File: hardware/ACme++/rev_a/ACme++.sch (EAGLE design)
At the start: 89 parts, among them J1 AC-PLUG, J2 WIRE_HOLE-14AWG, J3 TC2030-CTX-NL, J4 WIRE_HOLE-14AWG, J5 WIRE_HOLE-14AWG, K1 S216S01F, Q1 STGD5NB120SZT4, Q2 FDV301N, U1 ADE7753, U2 SR086SG-G, U3 TDA3664AT, U4 FM25LBTDFN-8, U5 CC2538, U6 DS2411, U7 TXB0104RGY, X1 ECS-35-17-5PX-TR, X2 EPSON-FA-128, X3 FC-12M32.7680KA-A3

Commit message: routing and labeling
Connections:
- net LOAD_PHASE: now also K1.1; no longer K1.2
- net WALL_PHASE: now also K1.2; no longer K1.1
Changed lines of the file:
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@@
+</segment>
+<segment>
+<pinref part="J1" gate="G$1" pin="PHASE"/>
+<wire x1="157.48" y1="170.18" x2="160.02" y2="170.18" width="0.1524" layer="91"/>
+<label x="160.02" y="170.18" size="1.27" layer="95" xref="yes"/>
+</segment>
+<segment>
+<pinref part="K1" gate="G$1" pin="2"/>
+<wire x1="63.5" y1="30.48" x2="66.04" y2="30.48" width="0.1524" layer="91"/>
+<label x="66.04" y="30.48" size="1.27" layer="95" xref="yes"/>
+</segment>
+</net>
+<net name="LOAD_PHASE" class="0">
+<segment>
+<pinref part="J2" gate="G$1" pin="P$1"/>
+<wire x1="220.98" y1="170.18" x2="218.44" y2="170.18" width="0.1524" layer="91"/>
+<label x="218.44" y="170.18" size="1.27" layer="95" rot="R180" xref="yes"/>
 </segment>
 <segment>
@@
 <label x="66.04" y="35.56" size="1.27" layer="95" xref="yes"/>
 </segment>
-<segment>
-<pinref part="J1" gate="G$1" pin="PHASE"/>
-<wire x1="157.48" y1="170.18" x2="160.02" y2="170.18" width="0.1524" layer="91"/>
-<label x="160.02" y="170.18" size="1.27" layer="95" xref="yes"/>
-</segment>
 </net>
-<net name="LOAD_PHASE" class="0">
-<segment>
-<pinref part="K1" gate="G$1" pin="2"/>
-<wire x1="63.5" y1="30.48" x2="66.04" y2="30.48" width="0.1524" layer="91"/>
-<label x="66.04" y="30.48" size="1.27" layer="95" xref="yes"/>
-</segment>
-<segment>
-<pinref part="J2" gate="G$1" pin="P$1"/>
-<wire x1="220.98" y1="170.18" x2="218.44" y2="170.18" width="0.1524" layer="91"/>
-<label x="218.44" y="170.18" size="1.27" layer="95" rot="R180" xref="yes"/>
-</segment>
-</net>

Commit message: added labels to schematic
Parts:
- added U$3: UMICH_SOLID_MEDIUM, logos:UMICH_SOLID_MEDIUM
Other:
- note added: "AC Plugs"
- note added: "ADE7753 Power Measurement"
- note added: "CC2538"
- note added: "DS2411"
- note added: "FRAM"
- note added: "Level Converter 5V SPI"
- note added: "Load Control Relay"
- note added: "Metering Conditioning"
- note added: "Programmer Header"
- note added: "Relay Control Switch and LED"

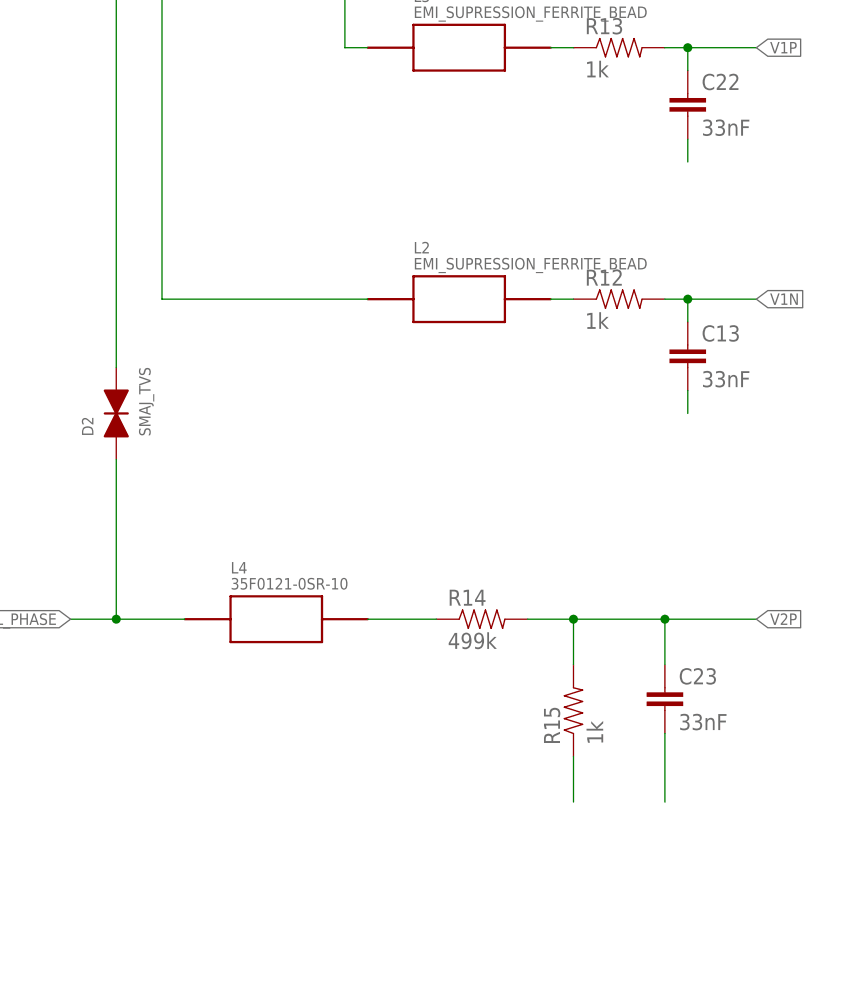
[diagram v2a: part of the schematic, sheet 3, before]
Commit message: changed gnd and routed
made the gnd for the ade measurement signals the emi filtered neutral
from the wall. As best as I can tell this is was acme does. Updated that
on the schematic and routed it.
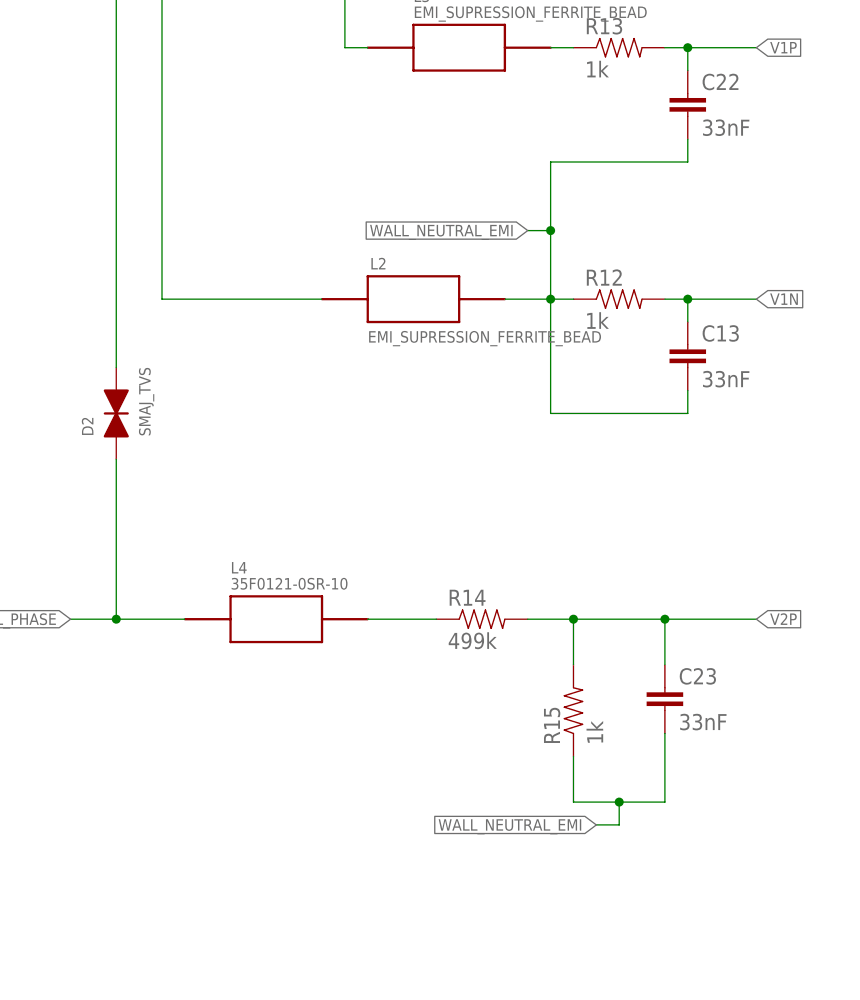
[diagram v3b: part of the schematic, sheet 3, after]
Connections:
- removed net N$14: L2.P$2, R12.1
- removed net N$19: C22.2
- removed net N$23: C13.2
- removed net N$25: C23.2
- removed net N$27: R15.1
- new net WALL_NEUTRAL_EMI: C13.2, C22.2, C23.2, L2.P$2, R12.1, R15.1
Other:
- moved on the sheet: L2
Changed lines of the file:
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@@
 <attribute name="DIGIKEY" x="152.4" y="157.48" size="1.27" layer="96" display="off"/>
 </instance>
-<instance part="L2" gate="G$1" x="177.8" y="119.38"/>
+<instance part="L2" gate="G$1" x="172.72" y="119.38" smashed="yes">
+<attribute name="NAME" x="167.894" y="122.682" size="1.27" layer="95"/>
+<attribute name="VALUE" x="167.64" y="114.554" size="1.27" layer="96"/>
+</instance>
 <instance part="L3" gate="G$1" x="177.8" y="147.32"/>
 <instance part="R12" gate="G$1" x="195.58" y="119.38">
@@
 <wire x1="144.78" y1="157.48" x2="139.7" y2="157.48" width="0.1524" layer="91"/>
 <wire x1="139.7" y1="157.48" x2="134.62" y2="157.48" width="0.1524" layer="91"/>
-<wire x1="167.64" y1="119.38" x2="144.78" y2="119.38" width="0.1524" layer="91"/>
+<wire x1="162.56" y1="119.38" x2="144.78" y2="119.38" width="0.1524" layer="91"/>
 <wire x1="144.78" y1="119.38" x2="144.78" y2="157.48" width="0.1524" layer="91"/>
 <junction x="144.78" y="157.48"/>
@@
 </segment>
 </net>
-<net name="N$14" class="0">
+<net name="WALL_NEUTRAL_EMI" class="0">
 <segment>
 <pinref part="L2" gate="G$1" pin="P$2"/>
 <pinref part="R12" gate="G$1" pin="1"/>
+<wire x1="182.88" y1="119.38" x2="187.96" y2="119.38" width="0.1524" layer="91"/>
 <wire x1="187.96" y1="119.38" x2="190.5" y2="119.38" width="0.1524" layer="91"/>
+<wire x1="187.96" y1="119.38" x2="187.96" y2="127" width="0.1524" layer="91"/>
+<wire x1="187.96" y1="127" x2="185.42" y2="127" width="0.1524" layer="91"/>
+<junction x="187.96" y="119.38"/>
+<label x="185.42" y="127" size="1.27" layer="95" rot="R180" xref="yes"/>
+<pinref part="C22" gate="G$1" pin="2"/>
+<wire x1="203.2" y1="137.16" x2="203.2" y2="134.62" width="0.1524" layer="91"/>
+<wire x1="187.96" y1="127" x2="187.96" y2="134.62" width="0.1524" layer="91"/>
+<wire x1="187.96" y1="134.62" x2="203.2" y2="134.62" width="0.1524" layer="91"/>
+<junction x="187.96" y="127"/>
+<pinref part="C13" gate="G$1" pin="2"/>
+<wire x1="203.2" y1="109.22" x2="203.2" y2="106.68" width="0.1524" layer="91"/>
+<wire x1="187.96" y1="119.38" x2="187.96" y2="106.68" width="0.1524" layer="91"/>
+<wire x1="187.96" y1="106.68" x2="203.2" y2="106.68" width="0.1524" layer="91"/>
+</segment>
+<segment>
+<pinref part="C23" gate="G$1" pin="2"/>
+<wire x1="200.66" y1="71.12" x2="200.66" y2="63.5" width="0.1524" layer="91"/>
+<pinref part="R15" gate="G$1" pin="1"/>
+<wire x1="190.5" y1="68.58" x2="190.5" y2="63.5" width="0.1524" layer="91"/>
+<wire x1="200.66" y1="63.5" x2="195.58" y2="63.5" width="0.1524" layer="91"/>
+<wire x1="195.58" y1="63.5" x2="190.5" y2="63.5" width="0.1524" layer="91"/>
+<wire x1="195.58" y1="63.5" x2="195.58" y2="60.96" width="0.1524" layer="91"/>
+<junction x="195.58" y="63.5"/>
+<wire x1="195.58" y1="60.96" x2="193.04" y2="60.96" width="0.1524" layer="91"/>
+<label x="193.04" y="60.96" size="1.27" layer="95" rot="R180" xref="yes"/>
 </segment>
 </net>
@@
 </segment>
 </net>
-<net name="N$19" class="0">
-<segment>
-<pinref part="C22" gate="G$1" pin="2"/>
-<wire x1="203.2" y1="137.16" x2="203.2" y2="134.62" width="0.1524" layer="91"/>
-</segment>
-</net>
-<net name="N$23" class="0">
-<segment>
-<pinref part="C13" gate="G$1" pin="2"/>
-<wire x1="203.2" y1="109.22" x2="203.2" y2="106.68" width="0.1524" layer="91"/>
-</segment>
-</net>
-<net name="N$25" class="0">
-<segment>
-<pinref part="C23" gate="G$1" pin="2"/>
-<wire x1="200.66" y1="71.12" x2="200.66" y2="63.5" width="0.1524" layer="91"/>
-</segment>
-</net>
-<net name="N$27" class="0">
-<segment>
-<pinref part="R15" gate="G$1" pin="1"/>
-<wire x1="190.5" y1="68.58" x2="190.5" y2="63.5" width="0.1524" layer="91"/>
-</segment>
-</net>

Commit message: routed ac under board, renamed
did my thing where part numbers correspond to values
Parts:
- added C36, C37: (no value), powercube:CAP_POL
- C1: value 0.1uF -> 12pF; device rcl:C-EUC0603 -> passives:CAPACITOR; DIGIKEY 445-1316-1-ND -> 445-1236-1-ND
- C10: value 0.1uF -> 33nF; device SparkFun-Passives:CAP0603-CAP -> SparkFun-Passives:CAP0805; DIGIKEY 445-1316-1-ND -> 478-1389-1-ND
- C11: value 47uF -> 0.1uF; device SparkFun-Passives:CAP1206 -> passives:CAPACITOR; DIGIKEY 399-5508-1-ND -> 445-1265-1-ND
- C12, C16: value 12pF -> 0.1uF; DIGIKEY 445-1236-1-ND -> 445-1265-1-ND
- C13: value 33nF -> 0.1uF; device SparkFun-Passives:CAP0805 -> passives:CAPACITOR; DIGIKEY 478-1389-1-ND -> 445-1265-1-ND
- C14: value 10uF -> 0.1uF; device rcl:C-EUC0603 -> passives:CAPACITOR; DIGIKEY (none) -> 445-1265-1-ND
- C15, C17: value 22pF -> 0.1uF; device rcl:C-EUC0603 -> passives:CAPACITOR; DIGIKEY (none) -> 445-1265-1-ND
- C18: value 1uF -> 0.1uF; DIGIKEY 445-4998-1-ND -> 445-1265-1-ND
- C2: value 10uF -> 12pF; device rcl:C-EUC0603 -> passives:CAPACITOR; DIGIKEY (none) -> 445-1236-1-ND
- C20, C21, C24: device passives:CAPACITOR -> SparkFun-Passives:CAP0603-CAP; DIGIKEY 445-1265-1-ND -> 445-1316-1-ND
- C22, C23: value 33nF -> 0.1uF; device SparkFun-Passives:CAP0805 -> SparkFun-Passives:CAP0603-CAP; DIGIKEY 478-1389-1-ND -> 445-1316-1-ND
- C25, C27: value 0.1uF -> 1uF; DIGIKEY 445-1265-1-ND -> 445-4998-1-ND
- C26: value 220pF -> 1uF; DIGIKEY 445-1251-1-ND -> 445-4998-1-ND
- C28: value 0.1uF -> 1uF; device passives:CAPACITOR -> SparkFun-Passives:CAP0603-CAP; DIGIKEY 445-1265-1-ND -> 445-5956-1-ND
- C29: device passives:CAPACITOR -> SparkFun-Passives:CAP1206; DIGIKEY 445-4998-1-ND -> 445-1381-1-ND
- C3: value 0.1uF -> 22pF; device rcl:C-EUC0603 -> passives:CAPACITOR; DIGIKEY 445-1316-1-ND -> 490-5868-1-ND
- C30: value 1uF -> 10uF; device passives:CAPACITOR -> SparkFun-Passives:CAP0603-CAP; DIGIKEY 445-4998-1-ND -> 1276-1119-1-ND
- C31: value 0.1uF -> 10uF; device passives:CAPACITOR -> SparkFun-Passives:CAP0603-CAP; DIGIKEY 445-1265-1-ND -> 1276-1119-1-ND
- C32: value 1nF -> 10uF; device passives:CAPACITOR -> SparkFun-Passives:CAP0603-CAP; DIGIKEY 445-2651-1-ND -> 1276-1119-1-ND
- C33: value 22pF -> 47uF; device passives:CAPACITOR -> SparkFun-Passives:CAP1206; DIGIKEY 490-5868-1-ND -> 399-5508-1-ND
- C34: value 22pF -> 470uF; device passives:CAPACITOR -> powercube:CAP_EEE-FP1E471AP; DIGIKEY 490-5868-1-ND -> (none)
- C4: value 10uF -> 22pF; device rcl:C-EUC0603 -> passives:CAPACITOR; DIGIKEY (none) -> 490-5868-1-ND
- C5: value 1uF -> 22pF; DIGIKEY 445-5956-1-ND -> 445-1273-1-ND
- C6: value 1uF -> 22pF; device SparkFun-Passives:CAP1206 -> SparkFun-Passives:CAP0603-CAP; DIGIKEY 445-1381-1-ND -> 445-1273-1-ND
- C7: value 470uF -> 220pF; device powercube:CAP_EEE-FP1E471AP -> passives:CAPACITOR; DIGIKEY (none) -> 445-1251-1-ND
- C8: value 0.1uF -> 33nF; device SparkFun-Passives:CAP0603-CAP -> SparkFun-Passives:CAP0805; DIGIKEY (none) -> 478-1389-1-ND
- C9: value 0.1uF -> 33nF; device rcl:C-EUC0603 -> SparkFun-Passives:CAP0805; DIGIKEY 445-1316-1-ND -> 478-1389-1-ND
- D1: value DIODE_MMBD914 -> SMAJ_TVS; device powercube:DIODE_MMBD914 -> powercube:SMAJ_TVS
- D2: value SMAJ_TVS -> CD2320-BB11000; device powercube:SMAJ_TVS -> powercube:CD2320-BB11000
- D3: value CD2320-BB11000 -> DIODE_MMBD914; device powercube:CD2320-BB11000 -> powercube:DIODE_MMBD914
- D4: value GREEN -> RED; DIGIKEY (none) -> 160-1835-1-ND
- D5: DIGIKEY (none) -> 160-1834-1-ND
- D6: value RED -> BLUE; DIGIKEY (none) -> 160-1837-1-ND
- J2: value WIRE_HOLE-14AWG -> TC2030-CTX-NL; device powercube:WIRE_HOLE-14AWG -> connector:TC2030-CTX-NL
- J3: value TC2030-CTX-NL -> WIRE_HOLE-14AWG; device connector:TC2030-CTX-NL -> powercube:WIRE_HOLE-14AWG
- R1: value 200k -> 0.001; device SparkFun-Resistors:RESISTOR1206 -> SparkFun-Resistors:RESISTOR2512; DIGIKEY P200KALCT-ND -> P1.0TCT-ND
- R10: value 100k -> 2.2k; device SparkFun:RESISTOR0603-RES -> passives:RESISTOR; DIGIKEY (none) -> RHM2.2KCECT-ND
- R11: value .001 -> 2.2k; device SparkFun-Resistors:RESISTOR2512 -> passives:RESISTOR; DIGIKEY P1.0TCT-ND -> RHM2.2KCECT-ND
- R12, R13: value 1k -> 4.7k; device SparkFun-Resistors:RESISTOR0805-RES -> passives:RESISTOR; DIGIKEY P16058CT-ND -> RHM4.7KCECT-ND
- R14: value 499k -> 4.7k; device SparkFun-Resistors:RESISTOR0805-RES -> passives:RESISTOR; DIGIKEY P499KCCT-ND -> RHM4.7KCECT-ND
- R15: value 1k -> 10k; device SparkFun-Resistors:RESISTOR0603-RES -> SparkFun:RESISTOR0603-RES; DIGIKEY RHM1.00KADCT-ND -> RHM10.0KCFCT-ND
- R16: value 4.7k -> 10k; device passives:RESISTOR -> SparkFun:RESISTOR0603-RES; DIGIKEY RHM4.7KCECT-ND -> RHM10.0KCFCT-ND
- R17: value 113k -> 12.4k; DIGIKEY (none) -> RHM12.4KCFCT-ND
- R18: value 12.4k -> 56k; device SparkFun-Resistors:RESISTOR0603-RES -> passives:RESISTOR; DIGIKEY RHM12.4KCFCT-ND -> RHM56KBHCT-ND
- R19: value 4.7k -> 100k; device passives:RESISTOR -> SparkFun:RESISTOR0603-RES; DIGIKEY RHM4.7KCECT-ND -> RHM100KCGCT-ND
- R2: value 200k -> 10; device SparkFun-Resistors:RESISTOR1206 -> SparkFun:RESISTOR0603-RES; DIGIKEY P200KALCT-ND -> RHM10.0CFCT-ND
- R20: value 2.2k -> 113k; device passives:RESISTOR -> SparkFun-Resistors:RESISTOR0603-RES; DIGIKEY RHM2.2KCECT-ND -> RHM113KCFCT-ND
- R21: value 56k -> 200k; device passives:RESISTOR -> SparkFun-Resistors:RESISTOR1206; DIGIKEY (none) -> P200KALCT-ND
- R22: value 2.2k -> 200k; device passives:RESISTOR -> SparkFun-Resistors:RESISTOR1206; DIGIKEY RHM2.2KCECT-ND -> P200KALCT-ND
- R23: value 470 -> 499k; device passives:RESISTOR -> SparkFun-Resistors:RESISTOR0805-RES; DIGIKEY RHM470BHCT-ND -> P499KCCT-ND
- R24, R25: value 470 -> 510k; device passives:RESISTOR -> SparkFun-Resistors:RESISTOR1206; DIGIKEY RHM470BHCT-ND -> P510KALCT-ND
- R3: value 4.7k -> 330; device passives:RESISTOR -> SparkFun-Resistors:RESISTOR0805-RES; DIGIKEY RHM4.7KCECT-ND -> RHM330KCT-ND
- R4, R5: value 510k -> 470; device SparkFun-Resistors:RESISTOR1206 -> passives:RESISTOR; DIGIKEY P510KALCT-ND -> RHM470BHCT-ND
- R6: value 10 -> 470; device SparkFun:RESISTOR0603-RES -> passives:RESISTOR; DIGIKEY (none) -> RHM470BHCT-ND
- R7: value 10k -> 1k; device SparkFun:RESISTOR0603-RES -> SparkFun-Resistors:RESISTOR0805-RES; DIGIKEY P10KGCT-ND -> P16058CT-ND
- R8: value 10k -> 1k; device SparkFun:RESISTOR0603-RES -> SparkFun-Resistors:RESISTOR0805-RES; DIGIKEY (none) -> P16058CT-ND
- R9: value (none) -> 1k; DIGIKEY RHM330KCT-ND -> P16058CT-ND
- S1: DIGIKEY (none) -> P11084SCT-ND
- U1: value ADE7753 -> CC2538; device powercube:ADE7753 -> chips:CC2538
- U2: value SR086SG-G -> DS2411; device powercube:SR086SG-G -> chips:DS2411
- U3: value TDA3664AT -> FM25LBTDFN-8; device powercube:TDA3664AT -> chips:FM25LBTDFN-8; DIGIKEY (none) -> FM25L04B-DGRA-ND; MOUSER (none) -> 877-FM25L04B-DG
- U4: value FM25LBTDFN-8 -> ADE7753; device chips:FM25LBTDFN-8 -> powercube:ADE7753; DIGIKEY FM25L04B-DGRA-ND -> (none); MOUSER 877-FM25L04B-DG -> 584-ADE7753ARSZR
- U5: value CC2538 -> TXB0104RGY; device chips:CC2538 -> chips:TXB0104RGY
- U6: value DS2411 -> SR086SG-G; device chips:DS2411 -> powercube:SR086SG-G
- U7: value TXB0104RGY -> TDA3664AT; device chips:TXB0104RGY -> powercube:TDA3664AT
- X1: value ECS-35-17-5PX-TR -> EPSON-FA-128; device powercube:ECS-35-17-5PX-TR -> crystals:EPSON-FA-128; DIGIKEY (none) -> SER3800CT-ND; MOUSER (none) -> 732-FA128-32F20X-K3
- X2: value EPSON-FA-128 -> FC-12M32.7680KA-A3; device crystals:EPSON-FA-128 -> crystals:FC-12M32.7680KA-A3; DIGIKEY SER3800CT-ND -> (none); MOUSER 732-FA128-32F20X-K3 -> (none)
- X3: value FC-12M32.7680KA-A3 -> ECS-35-17-5PX-TR; device crystals:FC-12M32.7680KA-A3 -> powercube:ECS-35-17-5PX-TR
- renumbered D7 to D5, L4 to L1
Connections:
- removed net N$5: C3.1, C4.1, R6.1, U1.AVDD
- new net ADE_AVDD: C21.1, C31.1, R2.1, U4.AVDD
- net !ADE_CS: now also U1.PB2, U5.A1; no longer U5.PB2, U7.A1
- net !ADE_CS_5V: now also U4.!CS, U5.B1; no longer U1.!CS, U7.B1
- net !ADE_IRQ: now also U1.PB1, U4.!IRQ; no longer U1.!IRQ, U5.PB1
- net !ADE_RESET: now also R16.2, U4.!RESET; no longer R8.2, U1.!RESET
- net !FRAM_CS: now also R12.1, U1.PC5, U3.!CS; no longer R3.1, U4.!CS, U5.PC5
- net !FRAM_HOLD: now also R13.1, U1.PC1, U3.!HOLD; no longer R16.1, U4.!HOLD, U5.PC1
- net !FRAM_WP: now also R14.1, U1.PC6, U3.!WP; no longer R19.1, U4.!WP, U5.PC6
- net !RESET: now also J2.!RESET, R11.1; no longer J3.!RESET, R20.1
- net 3V3: now also C11.1, C12.1, C13.1, C14.1, C15.1, C16.1, C17.1, C7.1, J2.VCC, R10.2, R12.2, R13.2, R14.2, R19.1, R4.1, R5.1, R6.1, U1.AVDD, U1.AVDD_GUARD, U1.DVDD, U2.VCC, U3.VDD, U5.OE, U5.VCCA, U6.VREG; no longer C18.1, C20.1, C21.1, C26.1, C27.1, C28.1, C31.1, C8.1, J3.VCC, R10.1, R16.2, R19.2, R22.2, R23.1, R24.1, R25.1, R3.2, U2.VREG, U4.VDD, U5.AVDD, U5.AVDD_GUARD, U5.DVDD, U6.VCC, U7.OE, U7.VCCA
- net 5V0: now also C20.1, C30.1, C33.1, R16.1, R2.2, R3.2, U4.DVDD, U5.VCCB, U7.VOUT; no longer C1.1, C11.1, C2.1, R6.2, R8.1, R9.2, U1.DVDD, U3.VOUT, U7.VCCB
- net ADE_CF: now also U1.PC7, U4.CF; no longer U1.CF, U5.PC7
- net ADE_ZX: now also U1.PB0, U4.ZX; no longer U1.ZX, U5.PB0
- net DC_RECTIFIED: now also D2.POS, R21.2, R24.2; no longer D3.POS, R1.2, R4.2
- net DS2411: now also R10.1, U1.PC0, U2.I/O; no longer R22.1, U5.PC0, U6.I/O
- net GND: now also C13.2, C22.2, C34.-, C7.2, D2.NEG, J2.GND, R15.1, R17.1, R18.2, R22.1, U1.GND, U3.VSS, U4.AGND, U4.DGND, U6.!EN, X1.GND; no longer C34.2, C7.-, C8.2, C9.2, D3.NEG, J3.GND, R18.1, R2.1, R21.2, R7.1, U1.AGND, U1.DGND, U2.!EN, U3.GND, U4.VSS, X2.GND
- net GREEN_LED: now also U1.PA6; no longer U5.PA6
- net LOAD_NEUTRAL: now also R1.2; no longer R11.2
- net LOAD_PHASE: now also J3.P$1; no longer J2.P$1
- net MISO: now also U1.PC4, U3.SO, U5.A3; no longer U4.SO, U5.PC4, U7.A3
- net MISO_5V: now also U4.DOUT, U5.B3; no longer U1.DOUT, U7.B3
- net MOSI: now also U1.PC3, U3.SI, U5.A4; no longer U4.SI, U5.PC3, U7.A4
- net MOSI_5V: now also U4.DIN, U5.B4; no longer U1.DIN, U7.B4
- net N$1: now also C26.1, C27.1, U1.DCOUPL1, U1.DCOUPL2; no longer C29.1, C30.1, U5.DCOUPL1, U5.DCOUPL2
- net N$10: now also C2.1, U1.XOSC32M_Q2, X1.2; no longer C16.1, U5.XOSC32M_Q2, X2.2
- net N$11: now also C22.1, C32.1, U4.REF; no longer C14.1, C9.1, U1.REF
- net N$12: now also D6.A, R6.2; no longer D4.A, R25.2
- net N$13: now also D3.1, R3.1; no longer D1.1, R9.1
- net N$15: now also C5.1, U4.CLKOUT, X3.P$2; no longer C17.1, U1.CLKOUT, X1.P$2
- net N$16: now also R7.1; no longer R13.1
- net N$17: now also R23.1; no longer R14.1
- net N$18: now also R21.1, R22.2; no longer R1.1, R2.2
- net N$2: now also C18.1, R11.2, U1.!RESET; no longer C32.1, R20.2, U5.!RESET
- net N$20: now also D4.A, R4.2; no longer D6.A, R23.2
- net N$21: now also R24.1, R25.2; no longer R4.1, R5.2
- net N$22: now also R5.2; no longer R24.2
- net N$24: now also C23.2, U6.VGD; no longer C10.2, U2.VGD
- net N$26: now also R17.2, R20.1, U6.FB; no longer R17.1, R18.2, U2.FB
- net N$3: now also C6.1, U4.CLKIN, X3.P$1; no longer C15.1, U1.CLKIN, X1.P$1
- net N$4: now also D3.2; no longer D1.2
- net N$6: now also C4.1, U1.PD7/XOSC32K_Q2, X2.2; no longer C34.1, U5.PD7/XOSC32K_Q2, X3.2
- net N$7: now also C3.1, U1.PD6/XOSC32K_Q1, X2.1; no longer C33.1, U5.PD6/XOSC32K_Q1, X3.1
- net N$8: now also R18.1, U1.R_BIAS; no longer R21.1, U5.R_BIAS
- net N$9: now also C1.1, U1.XOSC32M_Q1, X1.1; no longer C12.1, U5.XOSC32M_Q1, X2.1
- net RED_LED: now also D4.C, U1.PA7; no longer D6.C, U5.PA7
- net RELAY_CTRL: now also R19.2, U1.PB5; no longer R10.2, U5.PB5
- net RELAY_LED: now also D6.C, U1.PB4; no longer D4.C, U5.PB4
- net RF_N: now also U1.RF_N; no longer U5.RF_N
- net RF_P: now also U1.RF_P; no longer U5.RF_P
- net SCLK: now also U1.PC2, U3.SCK, U5.A2; no longer U4.SCK, U5.PC2, U7.A2
- net SCLK_5V: now also U4.SCLK, U5.B2; no longer U1.SCLK, U7.B2
- net SR086_GATE: now also U6.GATE; no longer U2.GATE
- net SR086_VIN: now also R25.1, U6.VIN; no longer R5.1, U2.VIN
- net TCK: now also J2.TCK, U1.JTAG_TCK; no longer J3.TCK, U5.JTAG_TCK
- net TDI: now also U1.PB6/JTAG-TDI; no longer U5.PB6/JTAG-TDI
- net TDO: now also J2.TDO, U1.PB7/JTAG-TDO; no longer J3.TDO, U5.PB7/JTAG-TDO
- net TMS: now also J2.TMS, U1.JTAG_TMS; no longer J3.TMS, U5.JTAG_TMS
- net USER_RELAY_CTRL: now also R15.2, U1.PB3; no longer R7.2, U5.PB3
- net V1N: now also C9.1, R8.2, U4.V1N, U4.V2N; no longer C13.1, R12.2, U1.V1N, U1.V2N
- net V1P: now also C8.1, R7.2, U4.V1P; no longer C22.1, R13.2, U1.V1P
- net V2P: now also C10.1, R23.2, R9.2, U4.V2P; no longer C23.1, R14.2, R15.2, U1.V2P
- net VDC: now also C23.1, C28.1, C29.1, C34.+, R20.2, U6.VOUT, U7.VIN; no longer C10.1, C5.1, C6.1, C7.+, R17.2, U2.VOUT, U3.VIN
- net WALL_NEUTRAL: now also D1.P$2, D2.AC2, R1.1; no longer D2.P$2, D3.AC2, R11.1
- net WALL_NEUTRAL_EMI: now also C10.2, C8.2, C9.2, R8.1, R9.1; no longer C13.2, C22.2, C23.2, R12.1, R15.1
- net WALL_PHASE: now also D1.P$1, D2.AC1; no longer D2.P$1, D3.AC1
